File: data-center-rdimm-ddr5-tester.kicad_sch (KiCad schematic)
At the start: 2 parts

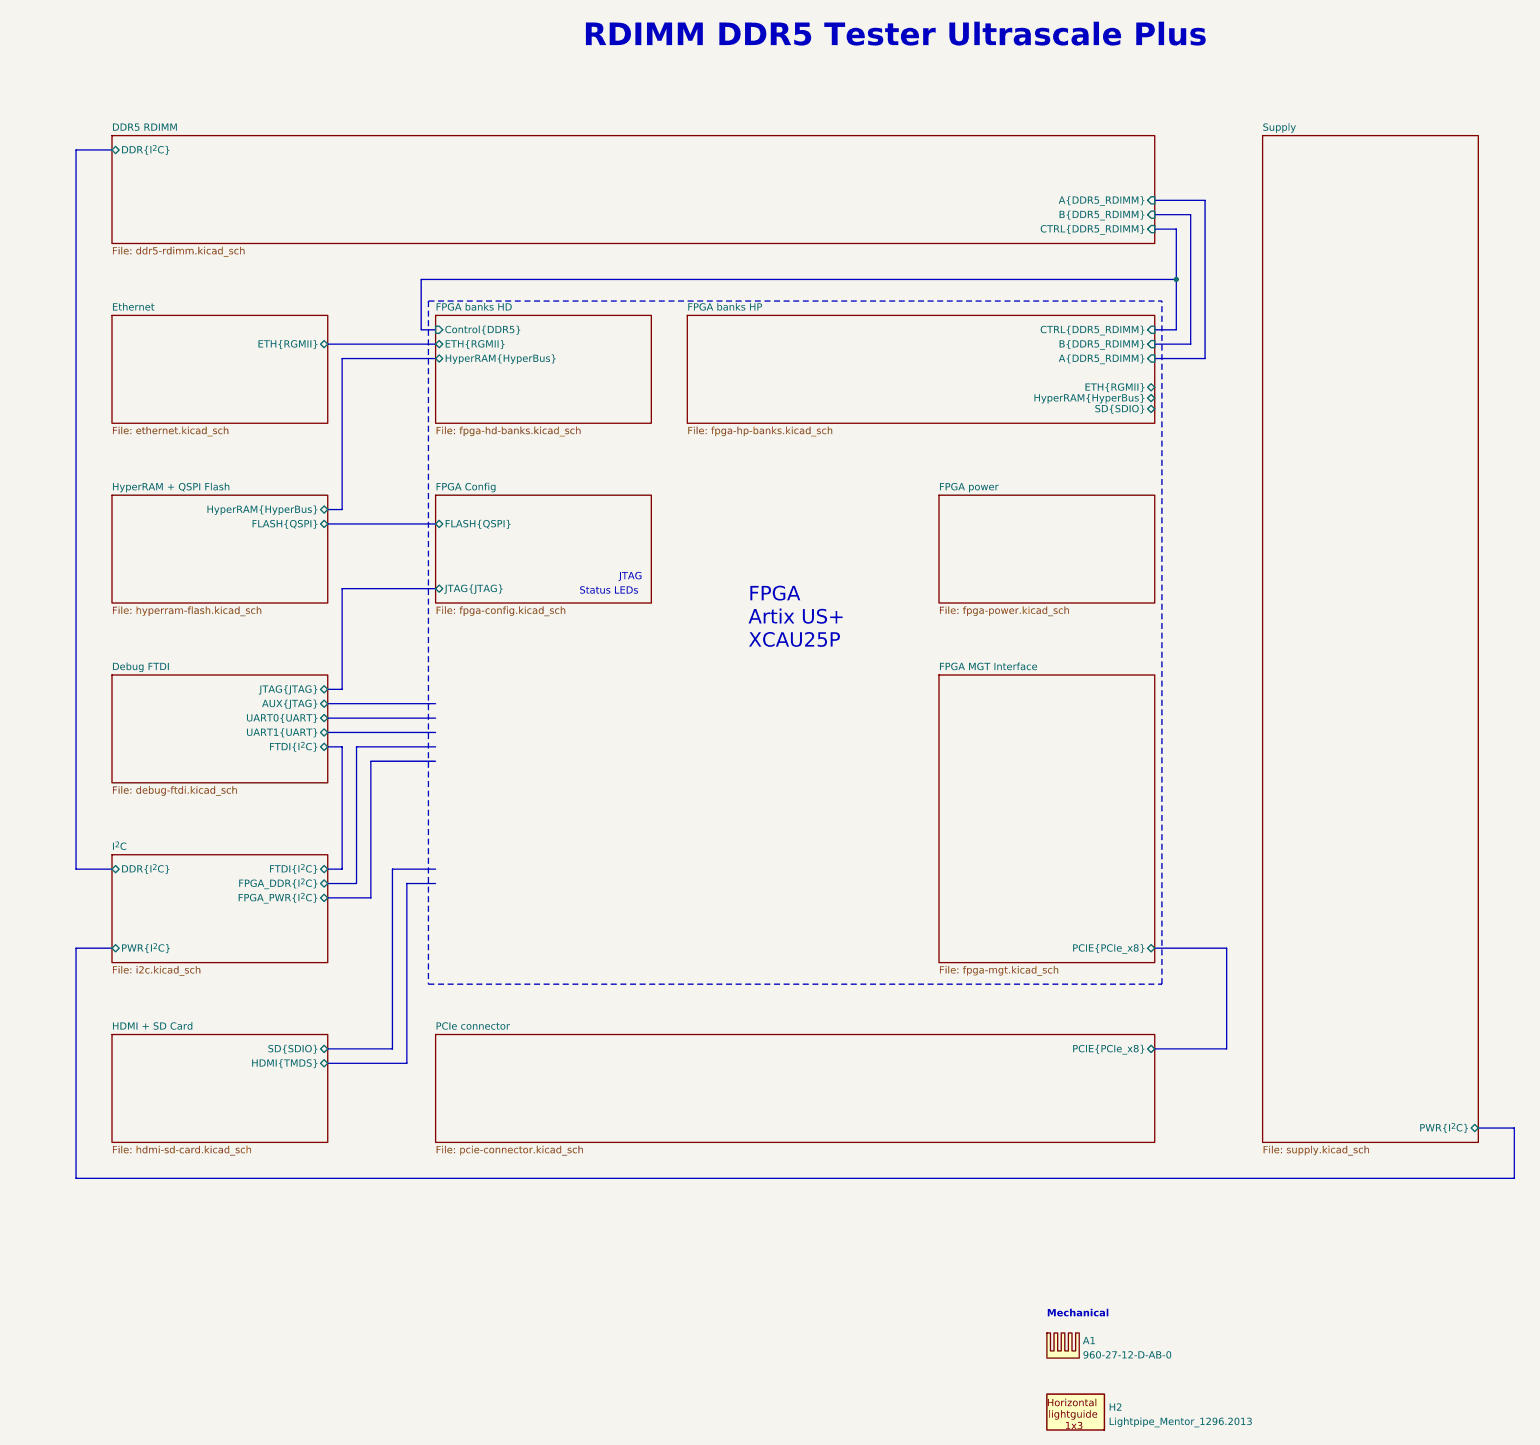
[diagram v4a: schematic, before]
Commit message: [#67016] Add RGMII, Hyper Ram and SD card schematic connection
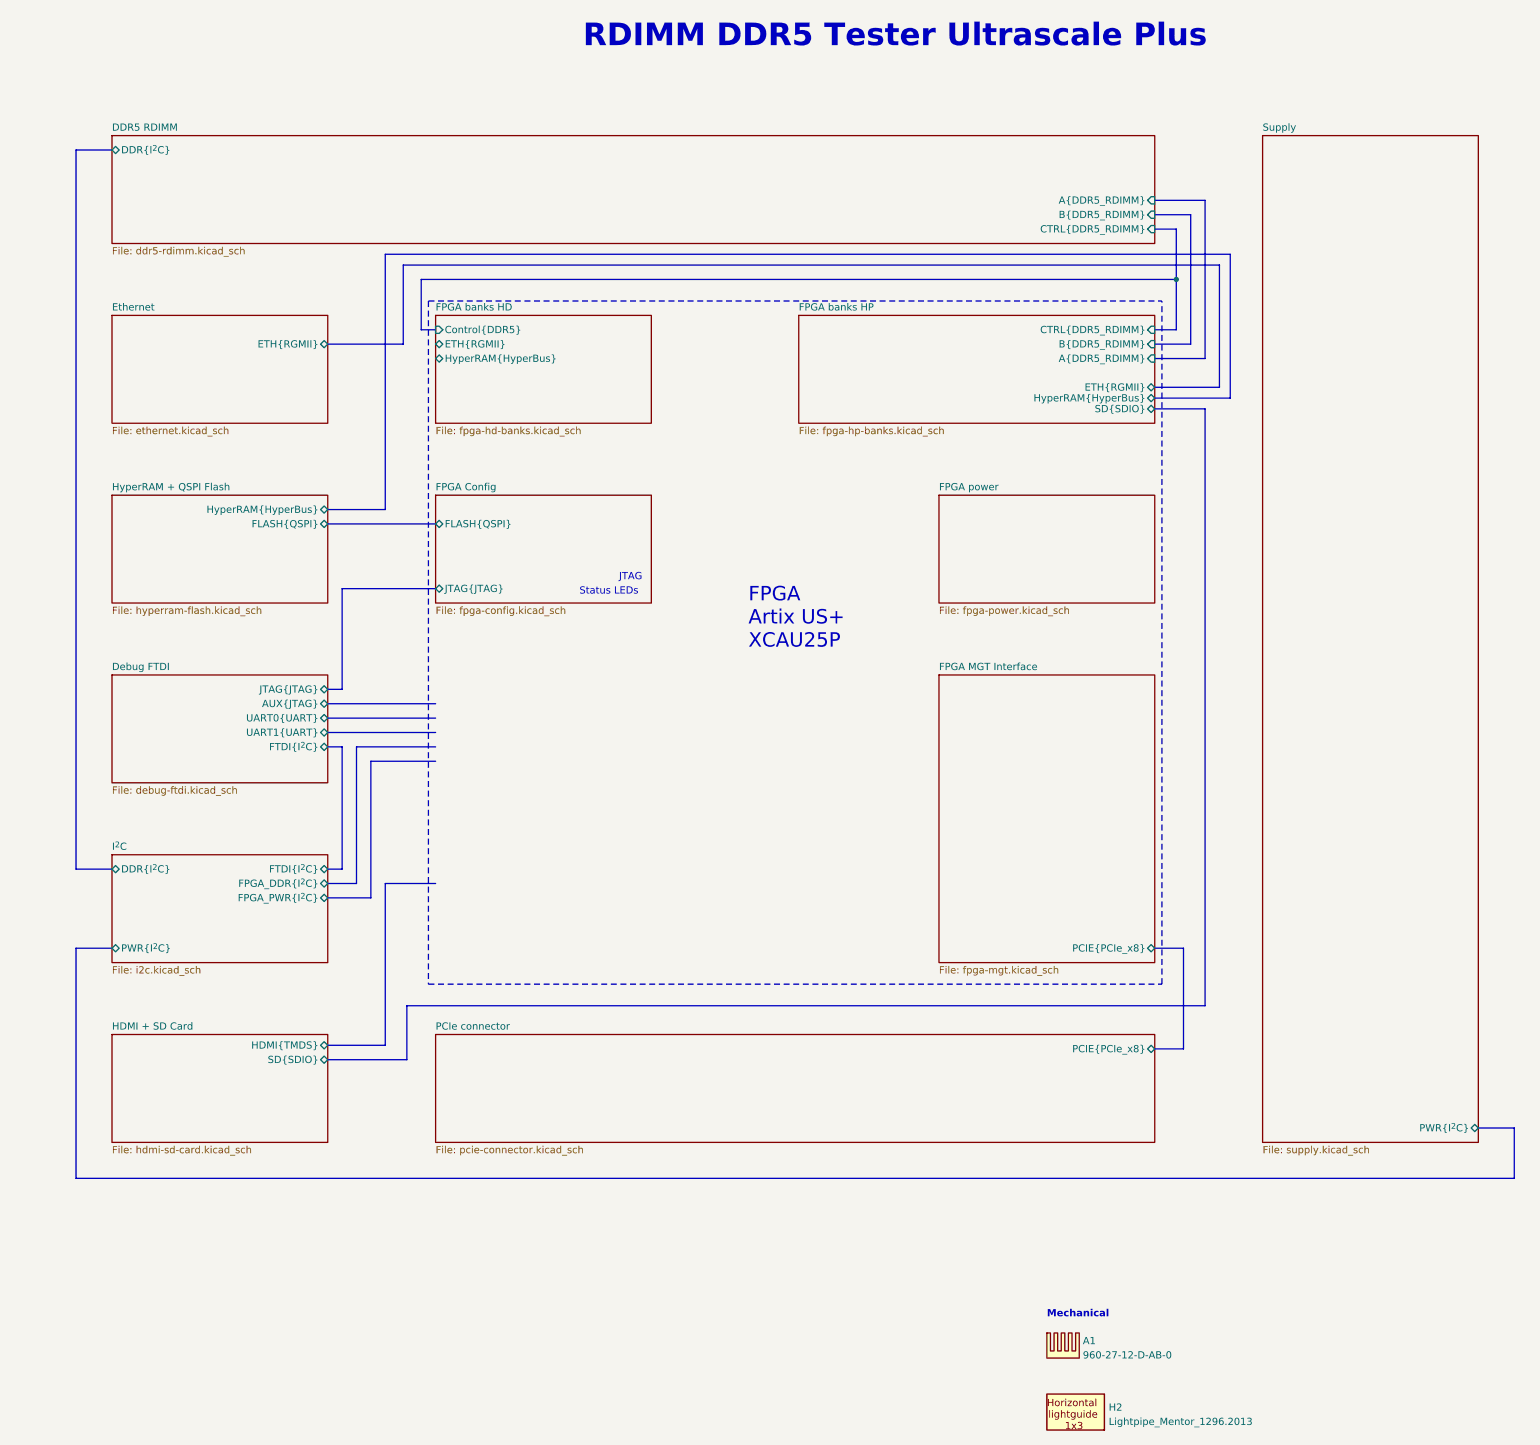
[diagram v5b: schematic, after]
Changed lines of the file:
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@@
   (junction (at 276.86 76.2) (diameter 0) (color 0 0 0 0)
   )
+  (bus (pts (xy 286.385 97.155) (xy 286.385 71.755))
+    (stroke (width 0) (type default) (color 208 190 93 1))
+  )
   (bus (pts (xy 127 153.67) (xy 146.05 153.67))
     (stroke (width 0) (type default))
   )
-  (bus (pts (xy 127 212.09) (xy 138.43 212.09))
-    (stroke (width 0) (type default))
-  )
-  (bus (pts (xy 140.97 182.88) (xy 140.97 214.63))
-    (stroke (width 0) (type default))
-  )
-  (bus (pts (xy 146.05 182.88) (xy 140.97 182.88))
+  (bus (pts (xy 140.335 87.63) (xy 140.335 73.66))
+    (stroke (width 0) (type default) (color 210 55 51 1))
+  )
+  (bus (pts (xy 127 213.995) (xy 140.97 213.995))
+    (stroke (width 0) (type default) (color 205 115 190 1))
+  )
+  (bus (pts (xy 137.16 182.88) (xy 137.16 211.455))
+    (stroke (width 0) (type default))
+  )
+  (bus (pts (xy 146.05 182.88) (xy 137.16 182.88))
     (stroke (width 0) (type default))
   )
@@
     (stroke (width 0) (type default))
   )
+  (bus (pts (xy 284.48 73.66) (xy 284.48 95.25))
+    (stroke (width 0) (type default) (color 210 55 51 1))
+  )
+  (bus (pts (xy 140.335 73.66) (xy 284.48 73.66))
+    (stroke (width 0) (type default) (color 210 55 51 1))
+  )
   (bus (pts (xy 82.55 234.95) (xy 336.55 234.95))
     (stroke (width 0) (type default))
@@
     (stroke (width 0) (type default))
   )
-  (bus (pts (xy 129.54 90.17) (xy 129.54 116.84))
-    (stroke (width 0) (type default))
+  (bus (pts (xy 137.16 71.755) (xy 137.16 116.84))
+    (stroke (width 0) (type default) (color 208 190 93 1))
   )
   (bus (pts (xy 279.4 87.63) (xy 273.05 87.63))
@@
     (stroke (width 0) (type default))
   )
-  (bus (pts (xy 129.54 116.84) (xy 127 116.84))
-    (stroke (width 0) (type default))
+  (bus (pts (xy 137.16 116.84) (xy 127 116.84))
+    (stroke (width 0) (type default) (color 208 190 93 1))
   )
   (bus (pts (xy 88.9 180.34) (xy 82.55 180.34))
     (stroke (width 0) (type default))
   )
+  (bus (pts (xy 127 87.63) (xy 140.335 87.63))
+    (stroke (width 0) (type default) (color 210 55 51 1))
+  )
   (bus (pts (xy 273.05 64.77) (xy 279.4 64.77))
     (stroke (width 0) (type default))
   )
   (bus (pts (xy 127 185.42) (xy 134.62 185.42))
-    (stroke (width 0) (type default))
-  )
-  (bus (pts (xy 146.05 90.17) (xy 129.54 90.17))
     (stroke (width 0) (type default))
   )
@@
     (stroke (width 0) (type default))
   )
-  (bus (pts (xy 285.75 212.09) (xy 273.05 212.09))
+  (bus (pts (xy 273.05 97.155) (xy 286.385 97.155))
+    (stroke (width 0) (type default) (color 208 190 93 1))
+  )
+  (bus (pts (xy 278.13 212.09) (xy 273.05 212.09))
     (stroke (width 0) (type default))
   )
@@
     (stroke (width 0) (type default))
   )
-  (bus (pts (xy 273.05 194.31) (xy 285.75 194.31))
-    (stroke (width 0) (type default))
-  )
-  (bus (pts (xy 140.97 214.63) (xy 127 214.63))
+  (bus (pts (xy 273.05 194.31) (xy 278.13 194.31))
+    (stroke (width 0) (type default))
+  )
+  (bus (pts (xy 137.16 211.455) (xy 127 211.455))
     (stroke (width 0) (type default))
   )
@@
     (stroke (width 0) (type default))
   )
-  (bus (pts (xy 127 87.63) (xy 146.05 87.63))
-    (stroke (width 0) (type default))
-  )
   (bus (pts (xy 276.86 85.09) (xy 273.05 85.09))
     (stroke (width 0) (type default))
@@
     (stroke (width 0) (type default))
   )
-  (bus (pts (xy 138.43 212.09) (xy 138.43 180.34))
-    (stroke (width 0) (type default))
+  (bus (pts (xy 281.94 99.06) (xy 281.94 204.47))
+    (stroke (width 0) (type default) (color 205 115 190 1))
   )
   (bus (pts (xy 82.55 180.34) (xy 82.55 53.34))
@@
     (stroke (width 0) (type default))
   )
-  (bus (pts (xy 285.75 194.31) (xy 285.75 212.09))
+  (bus (pts (xy 281.94 99.06) (xy 273.05 99.06))
+    (stroke (width 0) (type default) (color 205 115 190 1))
+  )
+  (bus (pts (xy 278.13 194.31) (xy 278.13 212.09))
     (stroke (width 0) (type default))
   )
@@
     (stroke (width 0) (type default))
   )
+  (bus (pts (xy 286.385 71.755) (xy 137.16 71.755))
+    (stroke (width 0) (type default) (color 208 190 93 1))
+  )
+  (bus (pts (xy 284.48 95.25) (xy 273.05 95.25))
+    (stroke (width 0) (type default) (color 210 55 51 1))
+  )
+  (bus (pts (xy 140.97 204.47) (xy 140.97 213.995))
+    (stroke (width 0) (type default) (color 205 115 190 1))
+  )
   (bus (pts (xy 82.55 194.31) (xy 82.55 234.95))
     (stroke (width 0) (type default))
   )
-  (bus (pts (xy 138.43 180.34) (xy 146.05 180.34))
-    (stroke (width 0) (type default))
+  (bus (pts (xy 140.97 204.47) (xy 281.94 204.47))
+    (stroke (width 0) (type default) (color 205 115 190 1))
   )
   (polyline (pts (xy 144.78 80.01) (xy 144.78 200.66))
@@
     )
   )
-  (sheet (at 190.5 82.55) (size 82.55 19.05) (fields_autoplaced)
+  (sheet (at 210.185 82.55) (size 62.865 19.05) (fields_autoplaced)
     (stroke (width 0) (type solid))
     (fill (color 0 0 0 0.0000))
-    (property "Sheetname" "FPGA banks HP" (at 190.5 81.8384 0)
+    (property "Sheetname" "FPGA banks HP" (at 210.185 81.8384 0)
       (effects (font (size 1.27 1.27)) (justify left bottom))
     )
-    (property "Sheetfile" "fpga-hp-banks.kicad_sch" (at 190.5 102.1846 0)
+    (property "Sheetfile" "fpga-hp-banks.kicad_sch" (at 210.185 102.1846 0)
       (effects (font (size 1.27 1.27)) (justify left top))
     )
@@
       (effects (font (size 1.27 1.27)) (justify left top))
     )
-    (pin "HDMI{TMDS}" bidirectional (at 127 214.63 0)
+    (pin "HDMI{TMDS}" bidirectional (at 127 211.455 0)
       (effects (font (size 1.27 1.27)) (justify right))
     )
-    (pin "SD{SDIO}" bidirectional (at 127 212.09 0)
+    (pin "SD{SDIO}" bidirectional (at 127 213.995 0)
       (effects (font (size 1.27 1.27)) (justify right))
     )
